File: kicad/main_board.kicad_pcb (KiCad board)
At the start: 2 copper layers, 42 x 67 mm, 56 parts, among them J1 Conn_01x07, J2 Conn_01x07, J3 Conn_01x07, J4 Conn_01x07, J5 Conn_01x07, J6 TYPE-C-31-M-12, J7 TYPE-C-31-M-12, J8 Conn_01x07, Q1 Q_NPN_BEC, Q2 Q_NPN_BEC, Q3 Q_NPN_BEC, Q4 Q_NPN_BEC, Q5 Q_NPN_BEC, SW1 Reset, SW2 Boot, U1 esp32-s2-wroom, U2 XC6220B331MR, U3 USBLC6-2SC6, U4 USBLC6-2SC6, U5 LMV324, U6 LMV324

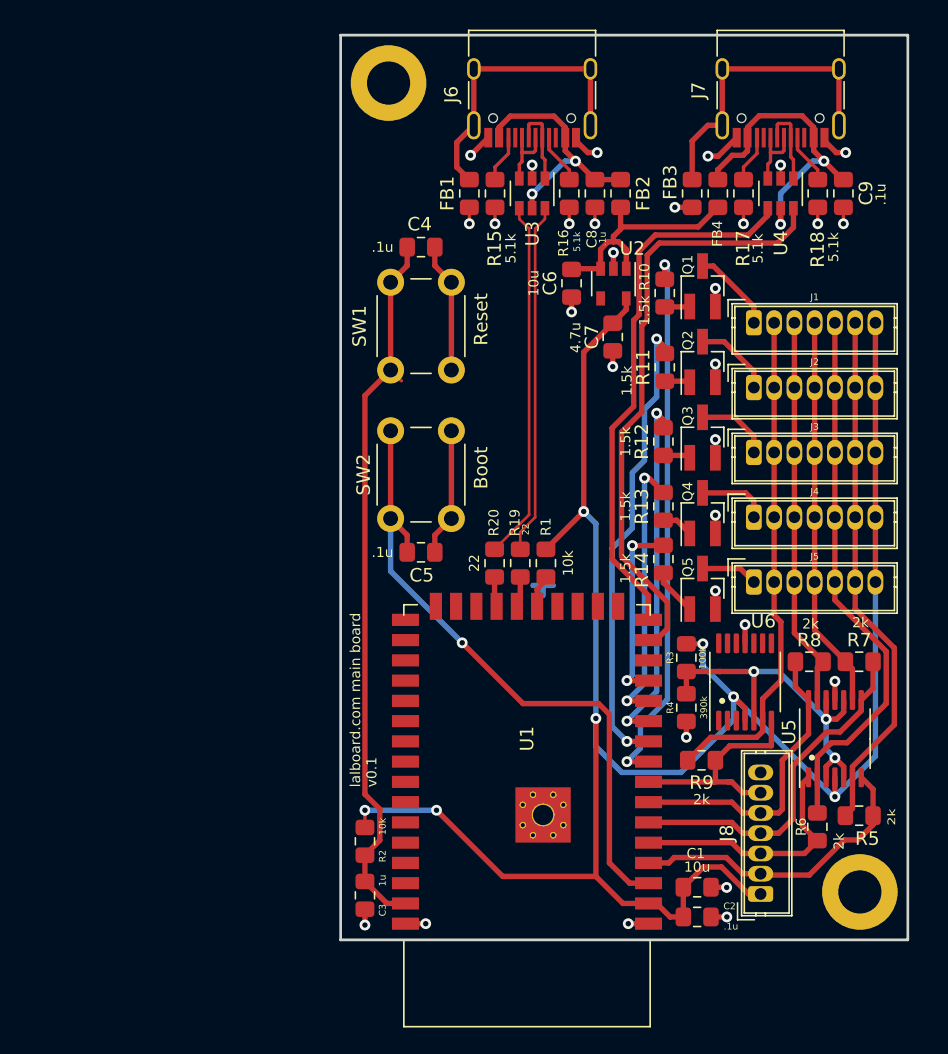
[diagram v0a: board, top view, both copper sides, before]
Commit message: wip: update mainboard with STM32
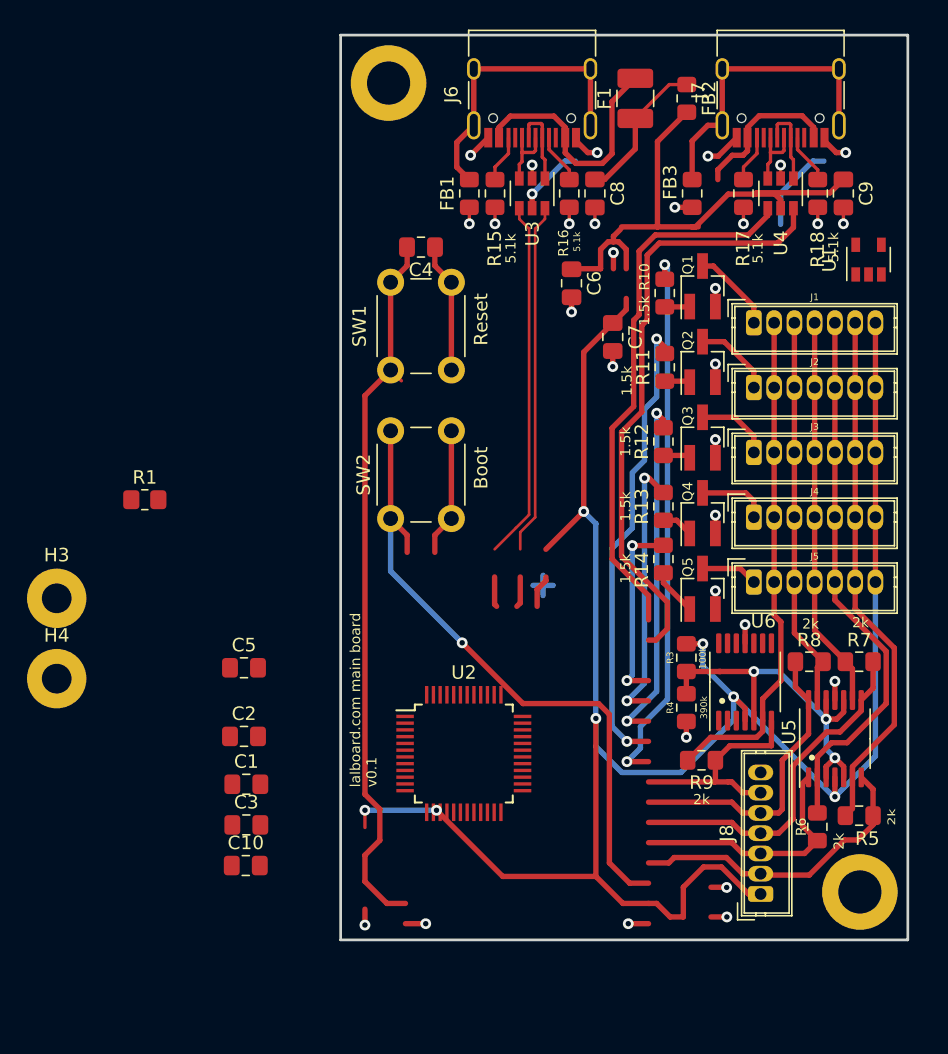
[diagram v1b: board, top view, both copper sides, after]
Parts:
- removed FB4: ACML-0805-500-T, Inductor_SMD:L_0805_2012Metric_Pad1.15x1.40mm_HandSolder
- removed R19, R20: 22, Resistor_SMD:R_0805_2012Metric_Pad1.15x1.40mm_HandSolder
- removed R2: 10k, Resistor_SMD:R_0805_2012Metric_Pad1.15x1.40mm_HandSolder
- added C10: 0.1u, Capacitor_SMD:C_0805_2012Metric_Pad1.18x1.45mm_HandSolder, F.Cu at (143.0, 94.5)
- added F1: Polyfuse 100mA, Fuse:Fuse_1210_3225Metric_Pad1.42x2.65mm_HandSolder, F.Cu at (171.8, 37.7)
- added H3: SWDIO, MountingHole:MountingHole_2.2mm_M2_Pad, F.Cu at (129.0, 74.7)
- added H4: SWCLK, MountingHole:MountingHole_2.2mm_M2_Pad, F.Cu at (129.0, 80.7)
- C1: value 10u -> 0.1u; footprint Capacitor_SMD:C_0805_2012Metric_Pad1.15x1.40mm_HandSolder -> Capacitor_SMD:C_0805_2012Metric_Pad1.18x1.45mm_HandSolder
- C2, C5: value .1u -> 0.1u; footprint Capacitor_SMD:C_0805_2012Metric_Pad1.15x1.40mm_HandSolder -> Capacitor_SMD:C_0805_2012Metric_Pad1.18x1.45mm_HandSolder
- C3: value 1u -> 0.1u; footprint Capacitor_SMD:C_0805_2012Metric_Pad1.15x1.40mm_HandSolder -> Capacitor_SMD:C_0805_2012Metric_Pad1.18x1.45mm_HandSolder
- C4, C8, C9: footprint Capacitor_SMD:C_0805_2012Metric_Pad1.15x1.40mm_HandSolder -> Capacitor_SMD:C_0805_2012Metric_Pad1.18x1.45mm_HandSolder
- C6: value 10u -> 1uF; footprint Capacitor_SMD:C_0805_2012Metric_Pad1.15x1.40mm_HandSolder -> Capacitor_SMD:C_0805_2012Metric_Pad1.18x1.45mm_HandSolder
- C7: value 4.7u -> 1uF; footprint Capacitor_SMD:C_0805_2012Metric_Pad1.15x1.40mm_HandSolder -> Capacitor_SMD:C_0805_2012Metric_Pad1.18x1.45mm_HandSolder
- R1: footprint Resistor_SMD:R_0805_2012Metric_Pad1.15x1.40mm_HandSolder -> Resistor_SMD:R_0805_2012Metric_Pad1.20x1.40mm_HandSolder
- U1: value esp32-s2-wroom -> MIC5504-3.3YM5; footprint lalboard:ESP32-S2-WROOM-handsoldering -> Package_TO_SOT_SMD:SOT-23-5
- U2: value XC6220B331MR -> STM32L412C8T6; footprint Package_TO_SOT_SMD:SOT-23-5 -> Package_QFP:TQFP-48_7x7mm_P0.5mm
- moved U1 43.5 mm to (189.1, 49.6), turned to 90 degrees
- moved U2 36.5 mm to (159.1, 86.2), turned to 0 degrees
- moved C2 36.1 mm to (142.8, 84.9)
- moved C1 34.2 mm to (143.0, 88.5)
- moved R1 30.1 mm to (135.5, 67.4), turned to 0 degrees
- moved C5 15.6 mm to (142.8, 79.8)
- moved C3 10.2 mm to (143.0, 91.5), turned to 0 degrees
- moved FB2 8.58 mm to (175.6, 37.7), turned to 270 degrees
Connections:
- net /U1RX_raw renamed /SCL_raw
- net /U1TX_raw renamed /SDA_raw
- C3 pad 1: /CHIP_PU -> +3V3
- C4 pad 2: /CHIP_PU -> /NRST
- C5 pad 1: /GPIO_0 -> +3V3
- C9 pad 1: Net-(C9-Pad1) -> +5V
- FB2 pad 1: +5V -> Net-(C8-Pad1)
- FB2 pad 2: Net-(C8-Pad1) -> +5V
- J1 pad 7: +3V3 -> +5V
- J2 pad 7: +3V3 -> +5V
- J3 pad 7: +3V3 -> +5V
- J4 pad 7: +3V3 -> +5V
- J5 pad 7: +3V3 -> +5V
- J6 pad A4: Net-(C8-Pad1) -> VBUS
- J6 pad A8: Net-(J6-PadA8) -> (no net)
- J6 pad A9: Net-(C8-Pad1) -> VBUS
- J6 pad B4: Net-(C8-Pad1) -> VBUS
- J6 pad B8: Net-(J6-PadB8) -> (no net)
- J6 pad B9: Net-(C8-Pad1) -> VBUS
- J7 pad A4: Net-(C9-Pad1) -> VBUS
- J7 pad A8: Net-(J7-PadA8) -> (no net)
- J7 pad A9: Net-(C9-Pad1) -> VBUS
- J7 pad B4: Net-(C9-Pad1) -> VBUS
- J7 pad B8: Net-(J7-PadB8) -> (no net)
- J7 pad B9: Net-(C9-Pad1) -> VBUS
- R1 pad 1: Net-(R1-Pad1) -> /BOOT0
- R1 pad 2: +3V3 -> GND
- SW1 pad 1: /CHIP_PU -> /NRST
- SW2 pad 1: /GPIO_0 -> /BOOT0
- SW2 pad 2: GND -> +3V3
- U1 pad 1: GND -> +5V
- U1 pad 2: +3V3 -> GND
- U1 pad 3: /GPIO_0 -> +5V
- U1 pad 4: /COL1_AMP -> (no net)
- U1 pad 5: /COL2_AMP -> +3V3
- U2 pad 1: +5V -> +3V3
- U2 pad 2: GND -> (no net)
- U2 pad 3: +5V -> (no net)
- U2 pad 4: Net-(U2-Pad4) -> (no net)
- U2 pad 5: +3V3 -> (no net)
- U3 pad 4: /D+ -> /USB_D+
- U3 pad 6: /D- -> /USB_D-
- U4 pad 4: /U1TX -> /I2C_SDA
- U4 pad 5: Net-(C9-Pad1) -> +5V
- U4 pad 6: /U1RX -> /I2C_SCL
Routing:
- net /NRST: track 0.00 -> 54.0 mm
- net /CHIP_PU: track 54.0 -> 0.00 mm
- net /GPIO_0: track 48.5 -> 0.00 mm, vias 1 -> 0
- net /BOOT0: track 0.00 -> 48.5 mm, vias 0 -> 1
- net /U1RX: track 44.7 -> 0.00 mm
- net /I2C_SCL: track 0.00 -> 44.7 mm
- net /U1TX: track 40.4 -> 0.00 mm
- net /I2C_SDA: track 0.00 -> 40.4 mm
- net VBUS: track 0.00 -> 30.2 mm
- net /USB_D+: track 0.00 -> 26.6 mm
- net /D+: track 26.6 -> 0.00 mm
- net /USB_D-: track 0.00 -> 26.0 mm
- net /D-: track 26.0 -> 0.00 mm
- net +5V: track 18.1 -> 39.0 mm
- net Net-(C9-Pad1): track 23.4 -> 6.49 mm, vias 2 -> 0
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- added copper zone on F.Cu, net GND
- removed copper zone on B.Cu, net GND

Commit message: Update kicad pcb data to change parts
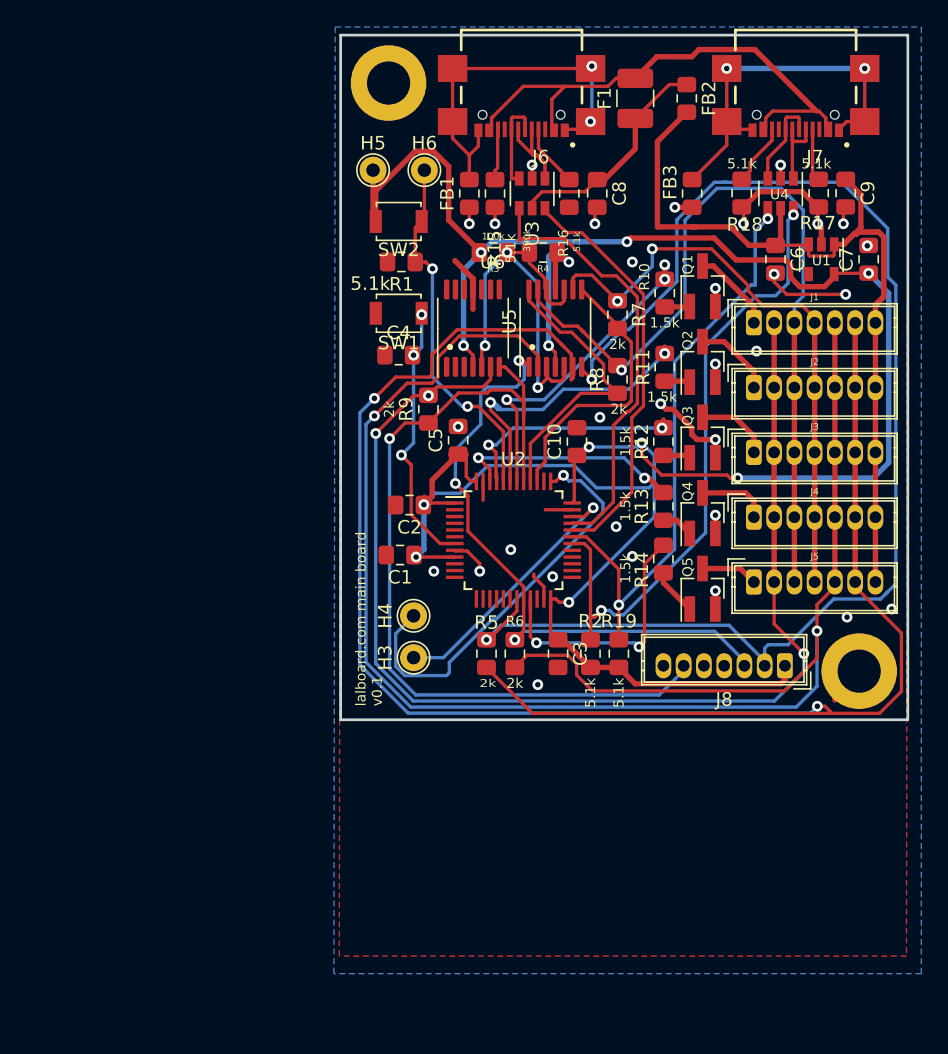
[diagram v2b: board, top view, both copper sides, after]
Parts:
- added H5: MountingHole_Pad, TestPoint:TestPoint_THTPad_D2.0mm_Drill1.0mm, F.Cu at (152.4, 43.0)
- added H6: MountingHole_Pad, TestPoint:TestPoint_THTPad_D2.0mm_Drill1.0mm, F.Cu at (156.2, 43.0)
- added R19: 5.1k, Resistor_SMD:R_0805_2012Metric_Pad1.15x1.40mm_HandSolder, F.Cu at (170.6, 78.8)
- added R2: 5.1k, Resistor_SMD:R_0805_2012Metric_Pad1.15x1.40mm_HandSolder, F.Cu at (168.5, 78.8)
- C1, C10, C2, C3, C4, C5, C6, C7, C8, C9: footprint Capacitor_SMD:C_0805_2012Metric_Pad1.18x1.45mm_HandSolder -> Capacitor_SMD:C_0805_2012Metric_Pad1.15x1.40mm_HandSolder
- H3, H4: footprint MountingHole:MountingHole_2.2mm_M2_Pad -> TestPoint:TestPoint_THTPad_D2.0mm_Drill1.0mm
- J6: value TYPE-C-31-M-12 -> USB-C; footprint Connector_USB:USB_C_Receptacle_HRO_TYPE-C-31-M-12 -> lalboard:GCT_USB4110-GF-A_REVB
- J7: footprint Connector_USB:USB_C_Receptacle_HRO_TYPE-C-31-M-12 -> lalboard:GCT_USB4110-GF-A_REVB
- R1: value 10k -> 5.1k; footprint Resistor_SMD:R_0805_2012Metric_Pad1.20x1.40mm_HandSolder -> Resistor_SMD:R_0805_2012Metric_Pad1.15x1.40mm_HandSolder
- SW1, SW2: footprint Button_Switch_THT:SW_PUSH_6mm_H5mm -> Button_Switch_SMD:SW_SPST_B3U-1000P
- moved C10 39.8 mm to (167.5, 63.1), turned to 90 degrees
- moved U5 36.8 mm to (165.9, 54.7)
- moved R4 35.3 mm to (165.0, 49.1), turned to 0 degrees
- moved R3 33.2 mm to (161.3, 49.1), turned to 0 degrees
- moved U6 33.1 mm to (159.8, 54.7)
- moved R9 32.9 mm to (156.5, 60.7), turned to 90 degrees
- moved R7 31.3 mm to (170.5, 53.7), turned to 90 degrees
- moved R5 30.1 mm to (160.8, 78.8), turned to 270 degrees
- moved H4 26.8 mm to (155.4, 76.0), turned to 180 degrees
- moved H3 26.8 mm to (155.4, 79.1), turned to 180 degrees
- moved C3 26.3 mm to (166.1, 78.8), turned to 270 degrees
- moved R1 25.9 mm to (154.5, 49.8), turned to 180 degrees
- moved R6 25.8 mm to (162.9, 78.8), turned to 270 degrees
- moved R8 25.3 mm to (170.5, 58.5), turned to 90 degrees
- moved C5 23.1 mm to (158.7, 63.0), turned to 90 degrees
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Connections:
- J6 pad A8: (no net) -> Net-(J6-PadA8)
- J6 pad B8: (no net) -> Net-(J6-PadB8)
- J7 pad A8: (no net) -> Net-(J7-PadA8)
- J7 pad B8: (no net) -> Net-(J7-PadB8)
- R17 pad 1: Net-(J7-PadB5) -> GND
- R17 pad 2: GND -> Net-(J7-PadA5)
- R18 pad 1: Net-(J7-PadA5) -> GND
- R18 pad 2: GND -> Net-(J7-PadB5)
- U1 pad 4: (no net) -> Net-(U1-Pad4)
- U2 pad 10: (no net) -> Net-(U2-Pad10)
- U2 pad 11: (no net) -> Net-(U2-Pad11)
- U2 pad 12: (no net) -> Net-(U2-Pad12)
- U2 pad 13: (no net) -> Net-(U2-Pad13)
- U2 pad 14: (no net) -> Net-(U2-Pad14)
- U2 pad 15: (no net) -> Net-(U2-Pad15)
- U2 pad 16: (no net) -> Net-(U2-Pad16)
- U2 pad 17: (no net) -> Net-(U2-Pad17)
- U2 pad 18: (no net) -> Net-(U2-Pad18)
- U2 pad 2: (no net) -> Net-(U2-Pad2)
- U2 pad 22: (no net) -> Net-(U2-Pad22)
- U2 pad 25: (no net) -> Net-(U2-Pad25)
- U2 pad 26: (no net) -> Net-(U2-Pad26)
- U2 pad 27: (no net) -> Net-(U2-Pad27)
- U2 pad 28: (no net) -> Net-(U2-Pad28)
- U2 pad 29: (no net) -> Net-(U2-Pad29)
- U2 pad 3: (no net) -> Net-(U2-Pad3)
- U2 pad 38: (no net) -> Net-(U2-Pad38)
- U2 pad 4: (no net) -> Net-(U2-Pad4)
- U2 pad 5: (no net) -> Net-(U2-Pad5)
- U2 pad 6: (no net) -> Net-(U2-Pad6)
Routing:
- net /COL1: track 39.2 -> 140.1 mm, vias 0 -> 2
- net /COL2: track 40.7 -> 125.6 mm, vias 0 -> 2
- net /COL1_AMP: track 22.7 -> 101.0 mm, vias 0 -> 2
- net /COL5: track 37.5 -> 89.5 mm, vias 0 -> 3
- net /COL5_AMP: track 16.7 -> 63.4 mm, vias 0 -> 1
- net +5V: track 39.0 -> 73.3 mm
- net /NRST: track 54.0 -> 19.8 mm, vias 0 -> 3
- net /COL4: track 29.0 -> 61.4 mm, vias 0 -> 1
- net /SWCLK: track 0.00 -> 31.1 mm, vias 0 -> 1
- net /COL2_AMP: track 18.7 -> 46.5 mm, vias 0 -> 3
- net +3V3: track 168.5 -> 192.8 mm, vias 7 -> 11
- net /BOOT0: track 48.5 -> 26.8 mm, vias 1 -> 2
- net /SWDIO: track 0.00 -> 19.7 mm, vias 0 -> 1
- net /ROW5: track 40.8 -> 23.1 mm, vias 2 -> 3
- net /COL3: track 29.1 -> 44.1 mm, vias 0 -> 2
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- added copper zone on B.Cu, net GND
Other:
- board size 42 x 67 mm -> 42 x 50.7 mm

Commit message: Customize
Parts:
- removed Q4, Q5: Q_NPN_BEC, Package_TO_SOT_SMD:SOT-23_Handsoldering
- added JP1: SolderJumper_2_Open, Jumper:SolderJumper-2_P1.3mm_Open_RoundedPad1.0x1.5mm, F.Cu at (153.6, 63.6)
- Q1, Q2, Q3: value Q_NPN_BEC -> Q_DUAL_NMOS_S1G1D2S2G2D1; footprint Package_TO_SOT_SMD:SOT-23_Handsoldering -> Package_TO_SOT_SMD:SOT-363_SC-70-6_Handsoldering
- R10, R11, R12, R13, R14: value 1.5k -> 5.1k
- moved Q3 11.2 mm to (175.5, 73.9)
- moved Q2 7.50 mm to (175.6, 64.6)
- moved R13 7.11 mm to (175.6, 61.0), turned to 0 degrees
- moved R11 6.77 mm to (175.5, 51.0), turned to 0 degrees
- moved R10 6.40 mm to (175.6, 58.3), turned to 180 degrees
- moved R12 5.38 mm to (175.6, 68.2), turned to 0 degrees
- moved Q1 3.23 mm to (175.6, 54.6)
- moved R14 2.27 mm to (175.6, 70.3), turned to 0 degrees
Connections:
- Q1 pad 1: Net-(Q1-Pad1) -> GND
- Q1 pad 2: GND -> /ROW5
- Q1 pad 3: Net-(J1-Pad1) -> Net-(J2-Pad1)
- Q2 pad 1: Net-(Q2-Pad1) -> GND
- Q2 pad 2: GND -> /ROW3
- Q2 pad 3: Net-(J2-Pad1) -> Net-(J4-Pad1)
- Q3 pad 1: Net-(Q3-Pad1) -> GND
- Q3 pad 2: GND -> /ROW1
- Q3 pad 3: Net-(J3-Pad1) -> GND
- R10 pad 1: Net-(Q1-Pad1) -> /ROW5
- R10 pad 2: /ROW5 -> GND
- R11 pad 1: Net-(Q2-Pad1) -> /ROW4
- R11 pad 2: /ROW4 -> GND
- R12 pad 1: Net-(Q3-Pad1) -> /ROW3
- R12 pad 2: /ROW3 -> GND
- R13 pad 1: Net-(Q4-Pad1) -> /ROW2
- R13 pad 2: /ROW2 -> GND
- R14 pad 1: Net-(Q5-Pad1) -> /ROW1
- R14 pad 2: /ROW1 -> GND
- R7 pad 1: /COL3_AMP -> /COL5_AMP
- R7 pad 2: /COL3 -> /COL5
- R9 pad 1: /COL5_AMP -> /COL3_AMP
- R9 pad 2: /COL5 -> /COL3
- U2 pad 39: /COL3_AMP -> /COL5_AMP
- U2 pad 41: /COL5_AMP -> /COL3_AMP
- U5 pad 8: /COL3_AMP -> /COL5_AMP
- U5 pad 9: /COL3 -> /COL5
- U6 pad 1: (no net) -> Net-(U6-Pad1)
- U6 pad 10: (no net) -> /AMP_REF
- U6 pad 12: (no net) -> /AMP_REF
- U6 pad 13: (no net) -> Net-(U6-Pad13)
- U6 pad 14: (no net) -> Net-(U6-Pad13)
- U6 pad 2: (no net) -> Net-(U6-Pad1)
- U6 pad 3: (no net) -> /AMP_REF
- U6 pad 6: /COL5 -> /COL3
- U6 pad 7: /COL5_AMP -> /COL3_AMP
- U6 pad 8: (no net) -> Net-(U6-Pad8)
- U6 pad 9: (no net) -> Net-(U6-Pad8)
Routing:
- net /COL5: track 89.5 -> 39.9 mm, vias 3 -> 2
- net /COL3: track 44.1 -> 88.9 mm
- net /COL5_AMP: track 63.4 -> 21.4 mm, vias 1 -> 0
- net +3V3: track 192.8 -> 178.0 mm, vias 11 -> 8
- net /ROW2: track 16.9 -> 29.2 mm
- net /ROW4: track 23.2 -> 33.5 mm
- net /AMP_REF: track 33.9 -> 42.5 mm, vias 3 -> 4
- net /ROW3: track 17.1 -> 22.1 mm
- net /ROW1: track 20.4 -> 24.9 mm
- net /ROW5: track 23.1 -> 27.1 mm, vias 3 -> 2
- net +5V: track 73.3 -> 69.7 mm
- net Net-(Q5-Pad1): track 3.48 -> 0.00 mm
- net Net-(J5-Pad1): track 4.21 -> 7.69 mm
- net GND: track 55.9 -> 59.2 mm, vias 32 -> 45
- net Net-(Q4-Pad1): track 2.35 -> 0.00 mm
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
